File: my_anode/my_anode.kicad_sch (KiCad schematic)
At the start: 5 parts, among them J1 7816-0000PR

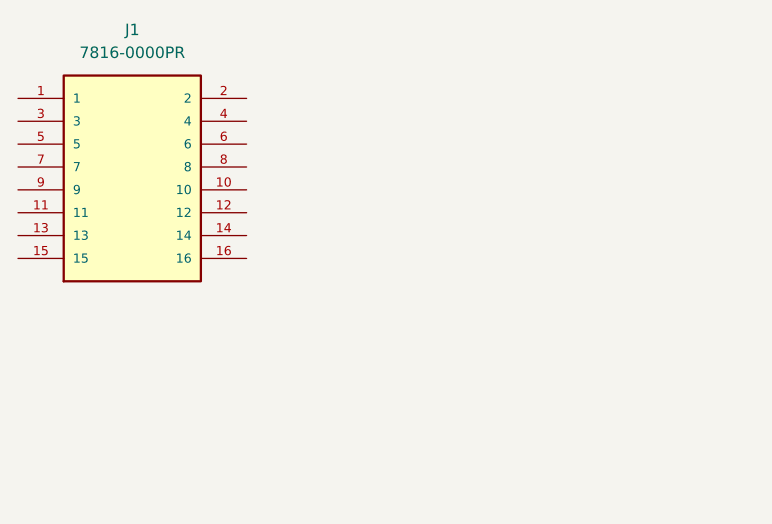
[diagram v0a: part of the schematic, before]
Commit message: Update anode work with mounting holes
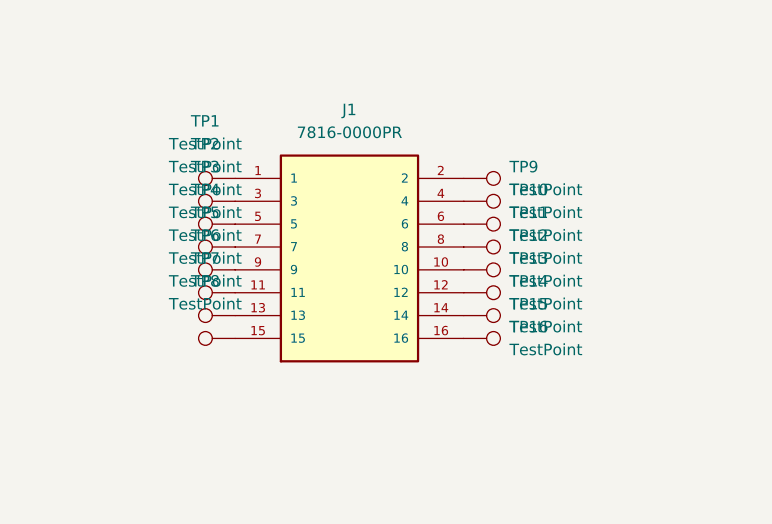
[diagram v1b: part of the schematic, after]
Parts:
- added TP1, TP10, TP11, TP12, TP13, TP14, TP15, TP16, TP2, TP3, TP4, TP5, TP6, TP7, TP8, TP9: TestPoint, TestPoint:TestPoint_Loop_D3.80mm_Drill2.0mm, symbol Connector:TestPoint
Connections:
- net at J1.1: now also TP1.1
- net at J1.10: now also TP13.1
- net at J1.11: now also TP6.1
- net at J1.12: now also TP14.1
- net at J1.13: now also TP7.1
- net at J1.14: now also TP15.1
- net at J1.15: now also TP8.1
- net at J1.16: now also TP16.1
- net at J1.2: now also TP9.1
- net at J1.3: now also TP2.1
- net at J1.4: now also TP10.1
- net at J1.5: now also TP3.1
- net at J1.6: now also TP11.1
- net at J1.7: now also TP4.1
- net at J1.8: now also TP12.1
- net at J1.9: now also TP5.1
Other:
- moved on the sheet: J1

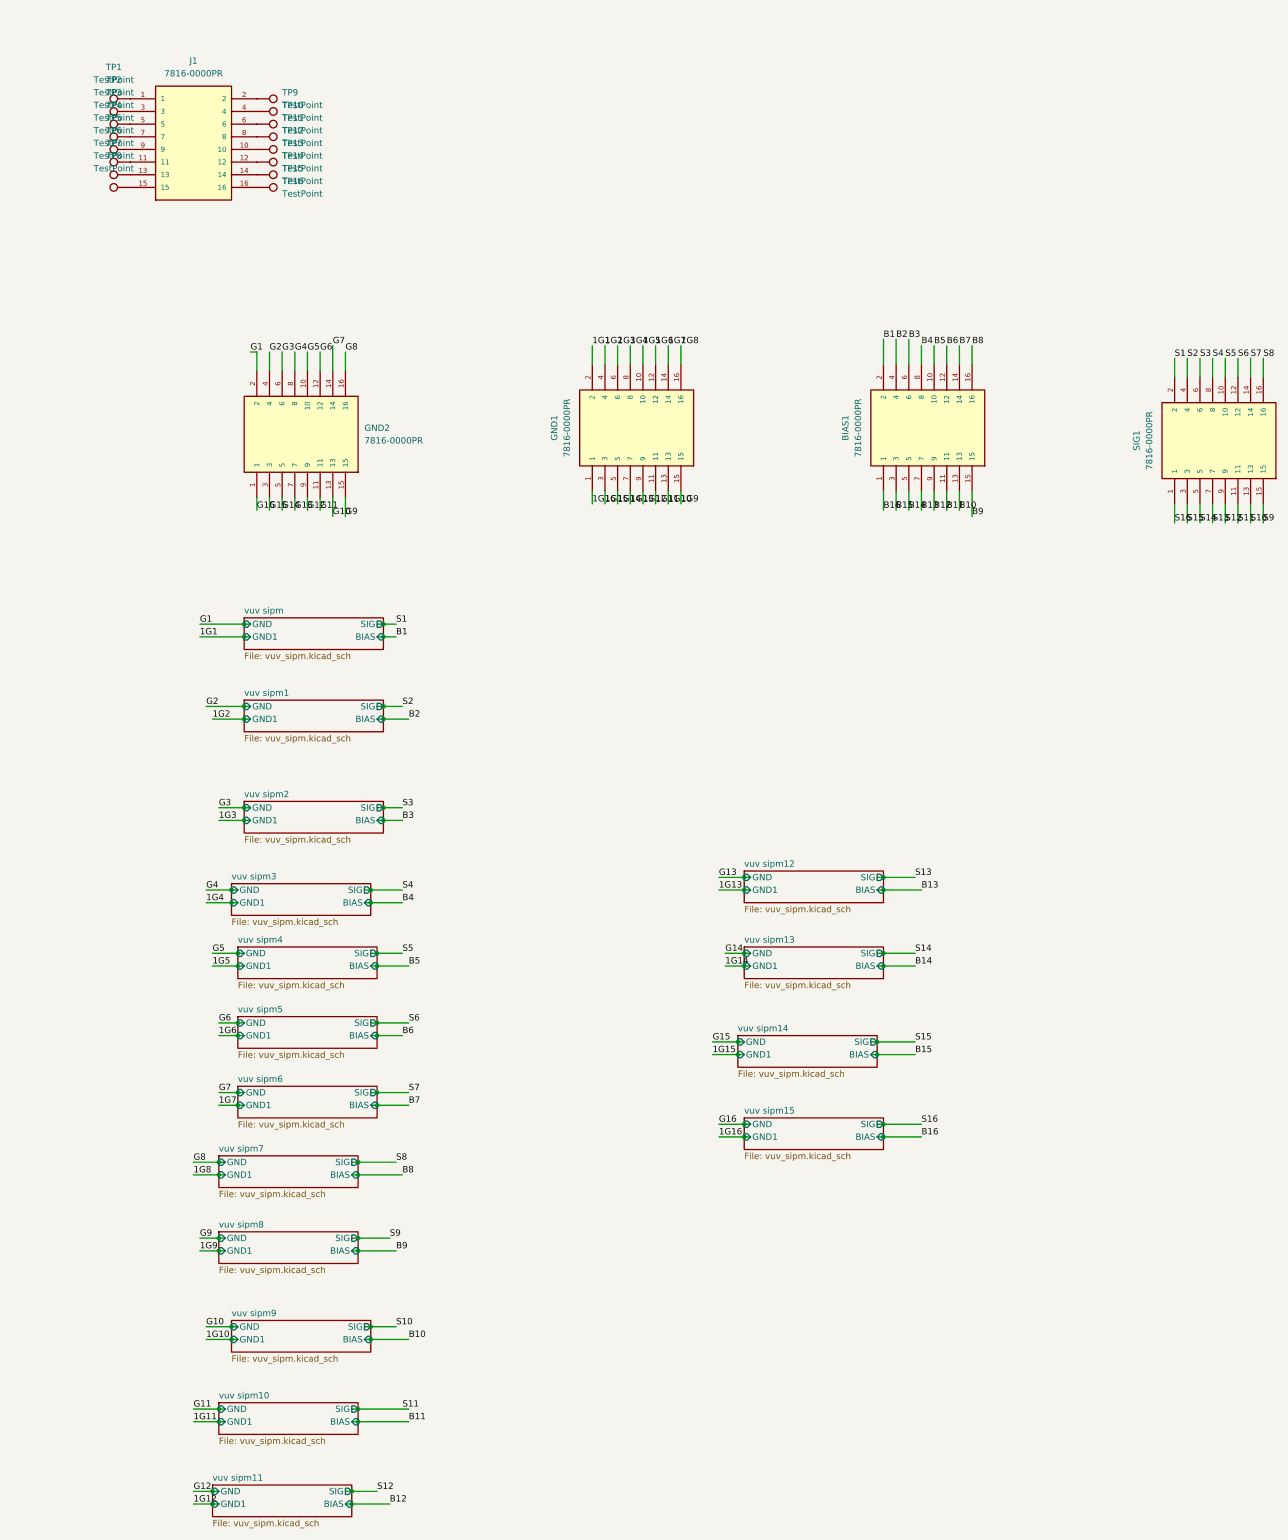
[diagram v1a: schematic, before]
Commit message: Add quarter-anode board
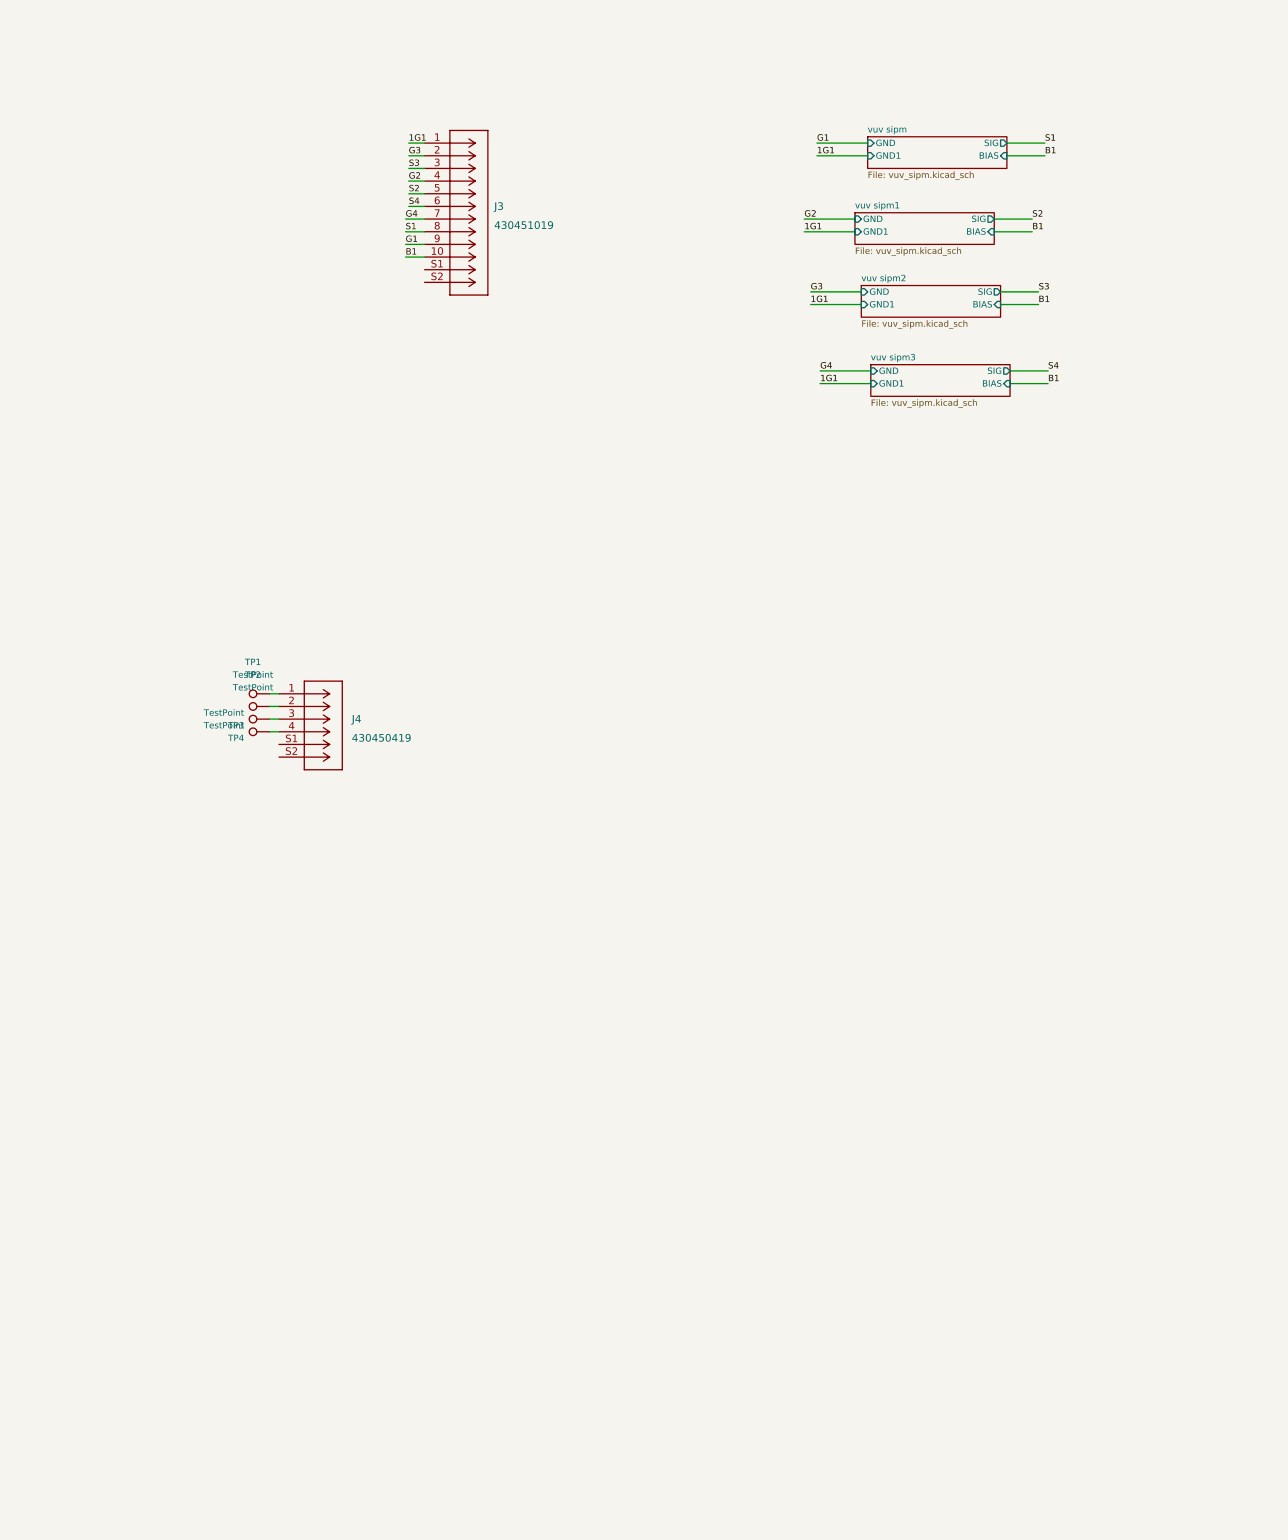
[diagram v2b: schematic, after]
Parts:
- removed BIAS1, GND1, GND2, J1, SIG1: 7816-0000PR, 7816-0000PR:3M_7816-0000PR, symbol 7816-0000PR:7816-0000PR
- removed TP10, TP11, TP12, TP13, TP14, TP15, TP16, TP5, TP6, TP7, TP8, TP9: TestPoint, TestPoint:TestPoint_Loop_D3.80mm_Drill2.0mm, symbol Connector:TestPoint
- added J3: 430451019, footprints:430451019, symbol 2023-02-26_21-05-37:430451019
- added J4: 430450419, 430450419:430450419, symbol 2023-02-26_21-14-33:430450419
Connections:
- net 1G1: now also J3.1
- net B1: now also J3.10
- net G1: now also J3.9
- net G2: now also J3.4
- net G3: now also J3.2
- net G4: now also J3.7
- net S1: now also J3.8
- net S2: now also J3.5
- net S3: now also J3.3
- net S4: now also J3.6
- net at TP4.1: now also J4.4
- net at TP2.1: now also J4.2
- net at TP1.1: now also J4.1
- net at TP3.1: now also J4.3
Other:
- removed sheet vuv sipm10
- removed sheet vuv sipm11
- removed sheet vuv sipm12
- removed sheet vuv sipm13
- removed sheet vuv sipm14
- removed sheet vuv sipm15
- removed sheet vuv sipm4
- removed sheet vuv sipm5
- removed sheet vuv sipm6
- removed sheet vuv sipm7
- removed sheet vuv sipm8
- removed sheet vuv sipm9
- moved on the sheet: TP1, TP2, TP3, TP4

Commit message: Add anode prior to copying
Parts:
- J2: renamed from J3; footprint footprints:430451019 -> 430451019:430451019
- renumbered J4 to J1
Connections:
- net G1: now also J2.3; no longer J2.9
- net G2: now also J2.5; no longer J2.4
- net G3: now also J2.7; no longer J2.2
- net G4: now also J2.9; no longer J2.7
- net S1: now also J2.2; no longer J2.8
- net S2: now also J2.4; no longer J2.5
- net S3: now also J2.6; no longer J2.3
- net S4: now also J2.8; no longer J2.6
- net 1G1: no longer names the net of J2.1
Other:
- sheet vuv sipm ports: added none; removed GND1
- sheet vuv sipm1 ports: added none; removed GND1
- sheet vuv sipm2 ports: added none; removed GND1
- sheet vuv sipm3 ports: added none; removed GND1
- moved on the sheet: J2
